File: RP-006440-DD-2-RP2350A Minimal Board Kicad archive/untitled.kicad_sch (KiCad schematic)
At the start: 39 parts, among them J5 USB_C_Receptacle_USB2.0_16P, SW3 SW_Push, SW4 SW_Push, U4 RP2350_60QFN, U5 NCP1117-3.3_SOT223, U6 W25Q128JVS, Y2 ABM8-272-T3

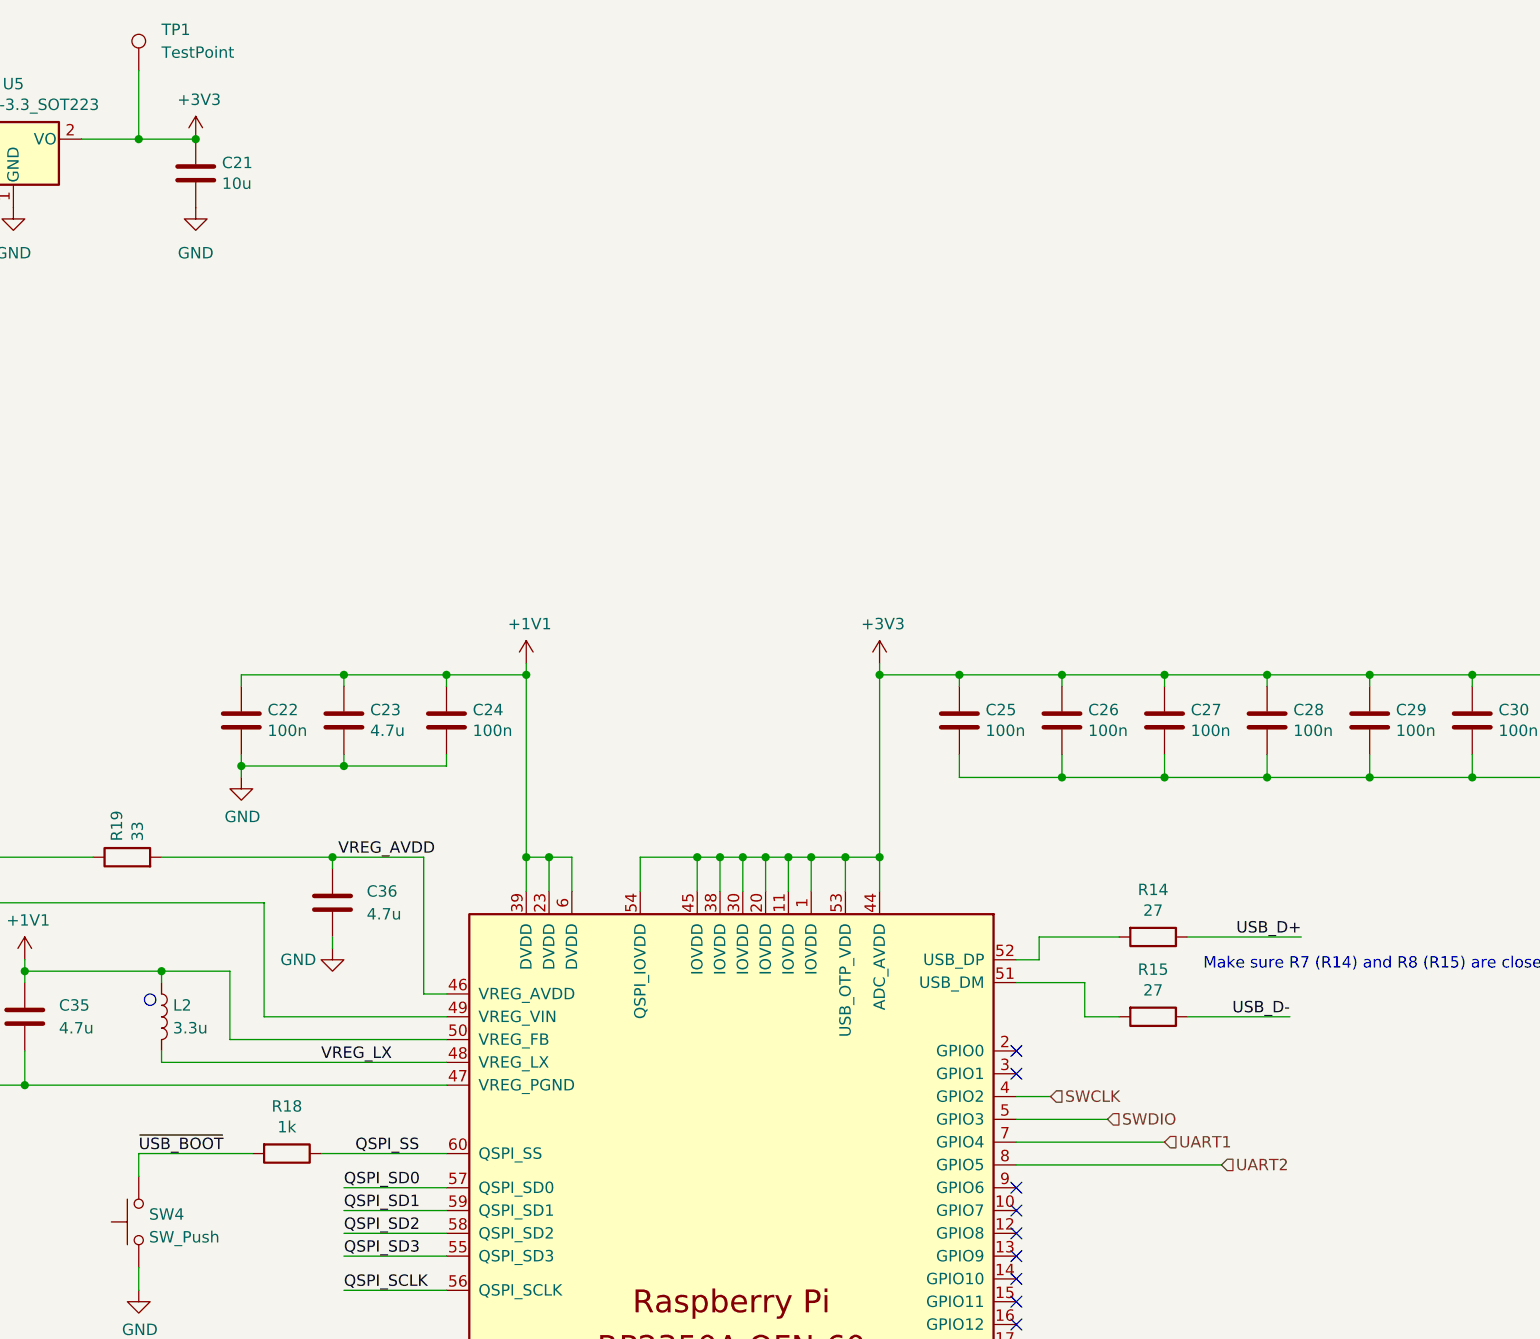
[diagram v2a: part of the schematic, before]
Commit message: Update schematic and PCB
Added hierarchal labels between main and debugprobe, connected the pins.
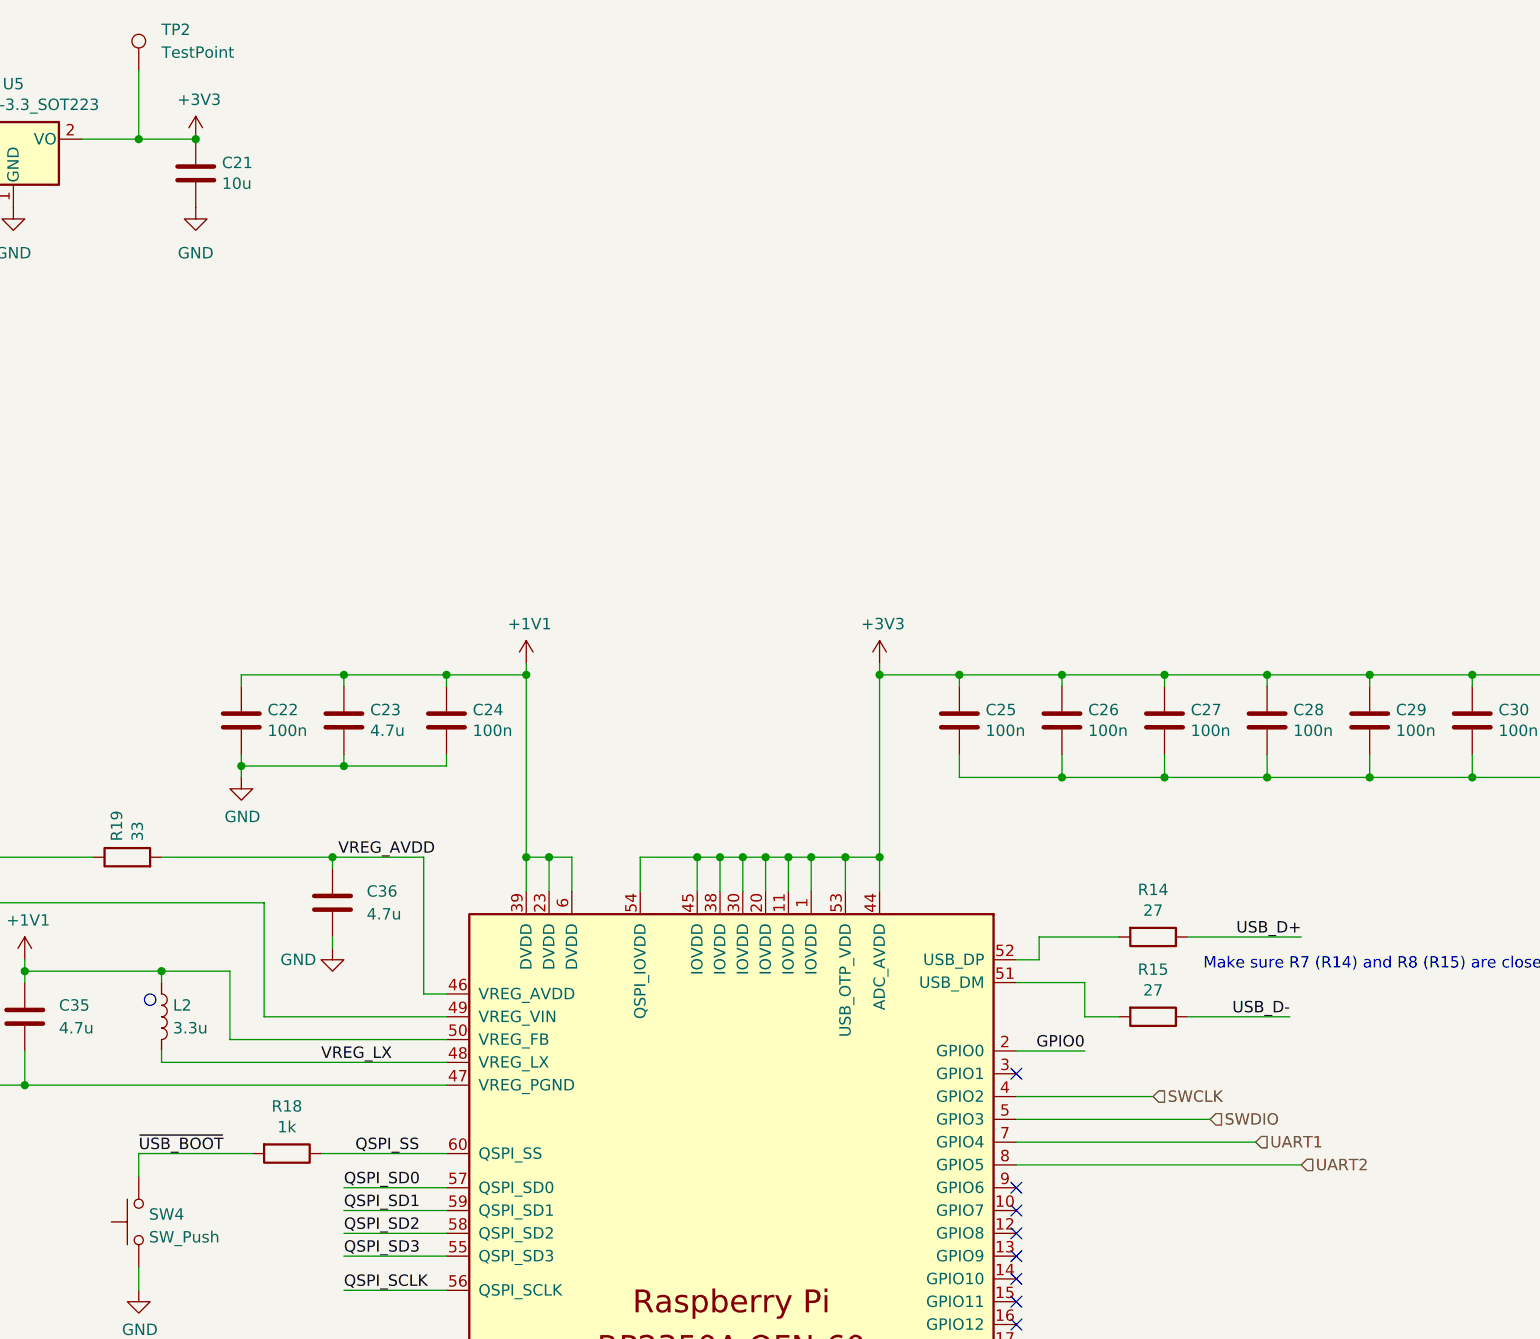
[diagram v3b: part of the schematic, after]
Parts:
- renumbered TP1 to TP2
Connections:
- net GPIO0: now also U4.2 (GPIO0)
- no-connect marks 28 -> 27
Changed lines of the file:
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@@
 	)
 	(no_connect
-		(at 222.25 139.7)
-	)
-	(no_connect
 		(at 222.25 154.94)
 	)
@@
 	(wire
 		(pts
-			(xy 245.11 152.4) (xy 222.25 152.4)
-		)
-		(stroke
-			(width 0)
-			(type default)
-		)
-	)
-	(wire
-		(pts
 			(xy 81.28 195.58) (xy 97.79 195.58)
 		)
@@
 	(wire
 		(pts
+			(xy 222.25 152.4) (xy 254 152.4)
+		)
+		(stroke
+			(width 0)
+			(type default)
+		)
+	)
+	(wire
+		(pts
 			(xy 186.69 118.11) (xy 189.23 118.11)
 		)
@@
 	(wire
 		(pts
-			(xy 238.76 149.86) (xy 222.25 149.86)
+			(xy 248.92 149.86) (xy 222.25 149.86)
 		)
 		(stroke
@@
 	(wire
 		(pts
-			(xy 226.06 144.78) (xy 222.25 144.78)
+			(xy 237.49 144.78) (xy 222.25 144.78)
 		)
 		(stroke
@@
 	(wire
 		(pts
+			(xy 222.25 139.7) (xy 229.87 139.7)
+		)
+		(stroke
+			(width 0)
+			(type default)
+		)
+	)
+	(wire
+		(pts
 			(xy 135.89 99.06) (xy 135.89 97.79)
 		)
@@
 	(wire
 		(pts
+			(xy 222.25 147.32) (xy 243.84 147.32)
+		)
+		(stroke
+			(width 0)
+			(type default)
+		)
+	)
+	(wire
+		(pts
 			(xy 194.31 118.11) (xy 196.85 118.11)
 		)
@@
 	(wire
 		(pts
-			(xy 232.41 147.32) (xy 222.25 147.32)
-		)
-		(stroke
-			(width 0)
-			(type default)
-		)
-	)
-	(wire
-		(pts
 			(xy 53.34 76.2) (xy 53.34 77.47)
 		)
@@
 		)
 	)
+	(label "GPIO0"
+		(at 229.87 139.7 180)
+		(effects
+			(font
+				(size 1.27 1.27)
+			)
+			(justify right bottom)
+		)
+	)
 	(label "QSPI_SD0"
 		(at 97.79 185.42 180)
@@
 		)
 	)
-	(hierarchical_label "UART1"
+	(hierarchical_label "UART2"
 		(shape input)
-		(at 238.76 149.86 0)
+		(at 254 152.4 0)
 		(effects
 			(font
@@
 		)
 	)
-	(hierarchical_label "SWCLK"
+	(hierarchical_label "SWDIO"
 		(shape input)
-		(at 226.06 144.78 0)
+		(at 243.84 147.32 0)
 		(effects
 			(font
@@
 		)
 	)
-	(hierarchical_label "SWDIO"
+	(hierarchical_label "SWCLK"
 		(shape input)
-		(at 232.41 147.32 0)
+		(at 237.49 144.78 0)
 		(effects
 			(font
@@
 		)
 	)
-	(hierarchical_label "UART2"
+	(hierarchical_label "UART1"
 		(shape input)
-		(at 245.11 152.4 0)
+		(at 248.92 149.86 0)
 		(effects
 			(font
@@
 		(dnp no)
 		(fields_autoplaced yes)
-		(property "Reference" "#PWR044"
+		(property "Reference" "#PWR065"
 			(at 85.09 41.91 0)
 			(effects
@@
 			(project ""
 				(path "/94683f5c-9cd9-448e-be96-9792537b5cb8/4bc304b2-df22-43ce-87c2-f3d7bd8364b0"
-					(reference "#PWR044")
+					(reference "#PWR065")
 					(unit 1)
 				)
@@
 		(dnp no)
 		(fields_autoplaced yes)
-		(property "Reference" "TP1"
+		(property "Reference" "TP2"
 			(at 127 25.9079 0)
 			(effects
@@
 		(pin "1"
 		)
-		(instances
-			(project ""
-				(path "/94683f5c-9cd9-448e-be96-9792537b5cb8/4bc304b2-df22-43ce-87c2-f3d7bd8364b0"
-					(reference "TP1")
-					(unit 1)
-				)
-			)
-		)
 	)

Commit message: Small change
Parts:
- renumbered TP2 to TP1
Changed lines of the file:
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@@
 		(dnp no)
 		(fields_autoplaced yes)
-		(property "Reference" "TP2"
+		(property "Reference" "TP1"
 			(at 127 25.9079 0)
 			(effects
@@
 		(pin "1"
 		)
+		(instances
+			(project "RP2350_60QFN_minimal"
+				(path "/94683f5c-9cd9-448e-be96-9792537b5cb8/4bc304b2-df22-43ce-87c2-f3d7bd8364b0"
+					(reference "TP1")
+					(unit 1)
+				)
+			)
+		)
 	)
